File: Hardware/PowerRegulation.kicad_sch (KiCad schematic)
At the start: 72 parts, among them Q3 AO3401A, Q4 AO3401A, U1 TPS56637RPAR, U14 AMS1117-3.3, U15 RT9193-33GB, U2 STUSB4500QTR, U8 STUSB4500QTR

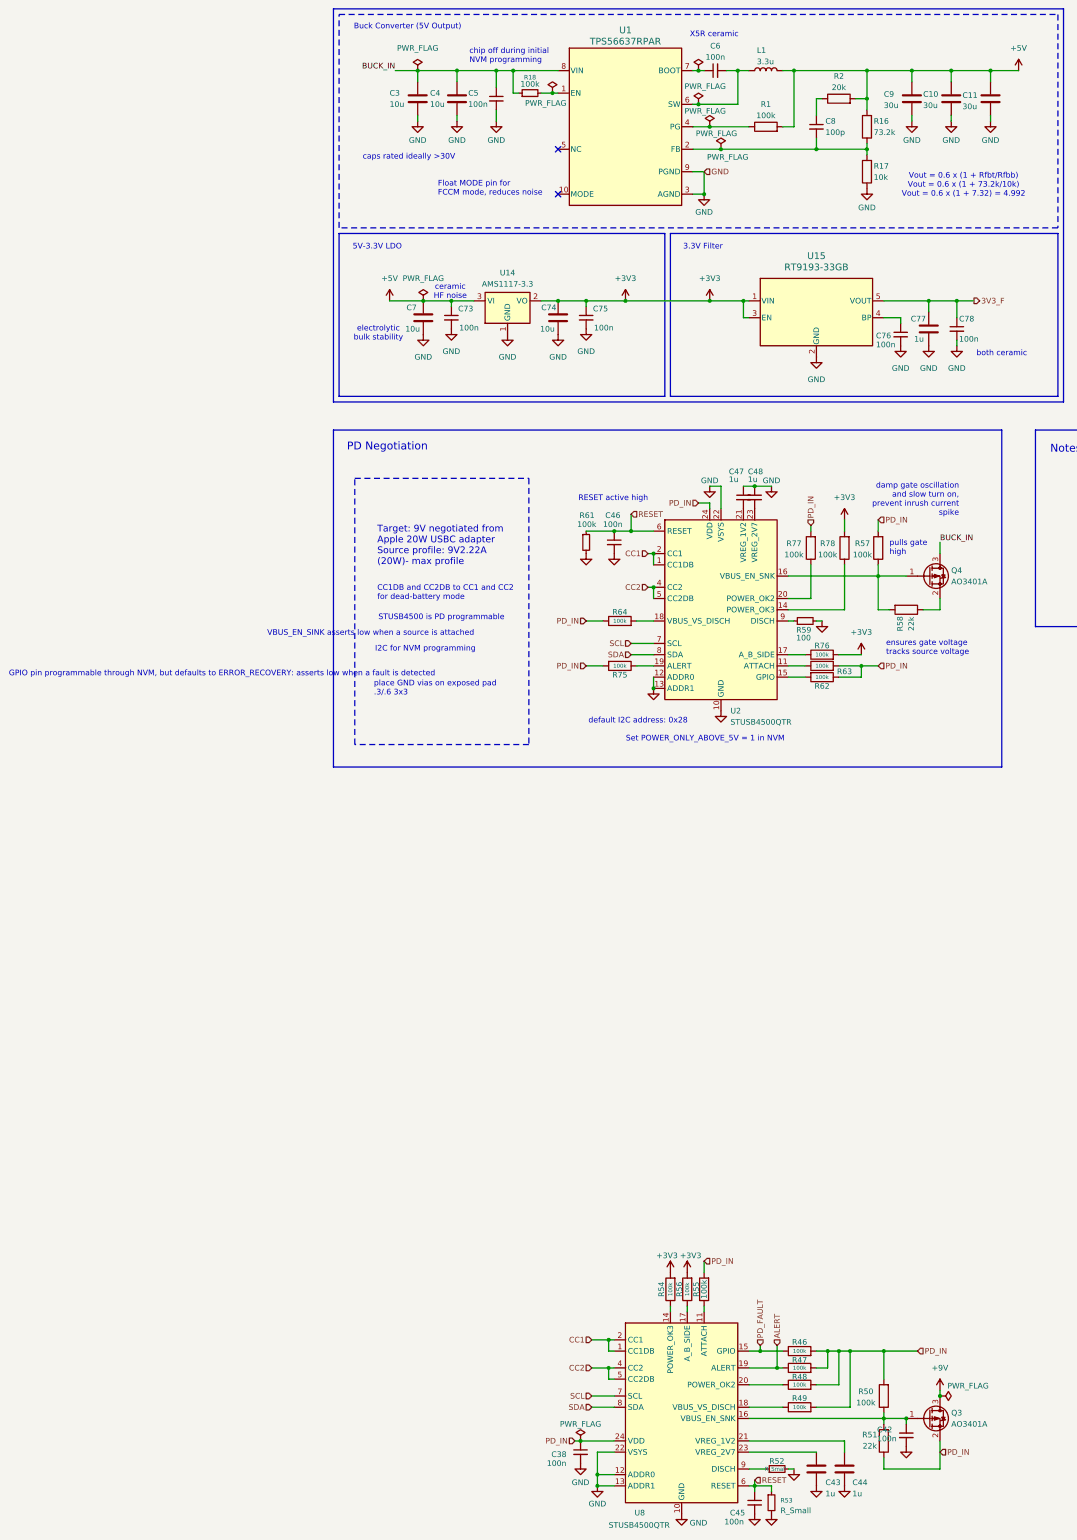
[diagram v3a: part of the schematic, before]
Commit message: added more testpoints and indicator LEDs, added application notes
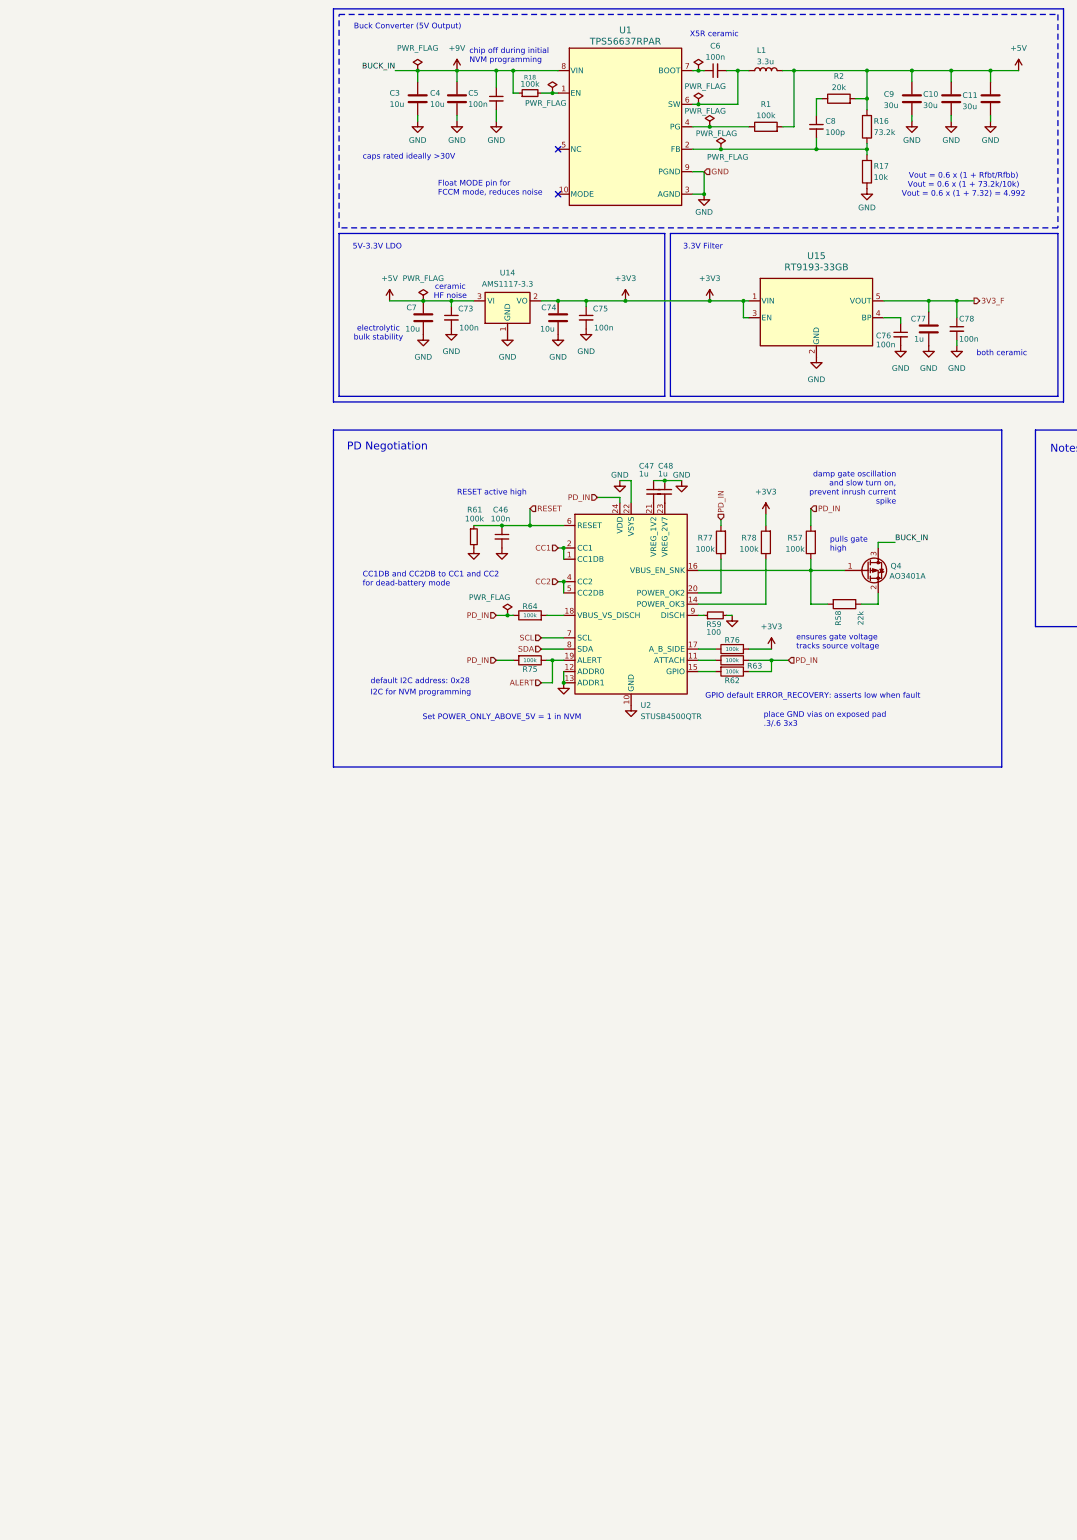
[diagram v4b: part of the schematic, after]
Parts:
- removed C38, C42, C45: 100n, symbol Device:C_Small
- removed C43, C44: 1u, symbol Device:C
- removed Q3: AO3401A, Package_TO_SOT_SMD:SOT-23, symbol Transistor_FET:AO3401A
- removed R46, R47, R48, R49, R50, R54, R55, R56: 100k, symbol Device:R
- removed R51: 22k, symbol Device:R
- removed R52, R53: R_Small, symbol Device:R_Small
- removed U8: STUSB4500QTR, Package_DFN_QFN:QFN-24-1EP_4x4mm_P0.5mm_EP2.7x2.7mm, symbol Interface_USB:STUSB4500QTR
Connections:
- net BUCK_IN is gone; now on net +9V: C3.1, C4.1, C5.1, Q4.3 (D), R18.1, U1.8 (VIN)
- net ALERT: now also R75.1, U2.19 (ALERT)
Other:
- note added: "GPIO default ERROR_RECOVERY: asserts low when fault"
- note removed: "GPIO pin programmable through NVM, but defaults to ERROR_RECOVERY: asserts low when a fault is detected"
- note removed: "STUSB4500 is PD programmable"
- note removed: "Target: 9V negotiated from Apple 20W USBC adapter Source profile: 9V2.22A (20W)- max profile"
- note removed: "VBUS_EN_SINK asserts low when a source is attached"
- moved on the sheet: C46, C47, C48, Q4, R57, R58, R59, R61, R62, R63, R64, R75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
